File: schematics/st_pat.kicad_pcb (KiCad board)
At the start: 2 copper layers, 23 parts, among them J4 BATTERY, SW1 SW_PWR, SW2 BTN_RST, SW3 BTN, SW4 BTN, SW5 BTN, U1 FGPMMOPA6H, U2 FEATHER_M0_BASIC_PROTO, U3 LIS2MDL_ADAFRUIT, U4 Sharp_Display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

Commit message: Re add routes
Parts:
- moved SW2 85.7 mm to (97.2, 93.3)
- moved U1 85.2 mm to (192.4, 77.5)
- moved C2 74.1 mm to (184.8, 62.9), turned to 270 degrees
- moved C1 71.5 mm to (181.0, 62.9), turned to 270 degrees
- moved D2 17.8 mm to (179.1, 93.8)
- moved R2 17.8 mm to (186.7, 94.2)
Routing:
- net +3V3: track 0.00 -> 271.3 mm
- net /RST: track 0.00 -> 202.6 mm
- net /MOSI: track 0.00 -> 174.1 mm, vias 0 -> 2
- net /SCK: track 0.00 -> 170.4 mm, vias 0 -> 2
- net /MISO: track 0.00 -> 153.8 mm, vias 0 -> 2
- net /GPS_FIX_D11: track 0.00 -> 116.5 mm
- net /GPS_TX: track 0.00 -> 100.1 mm, vias 0 -> 1
- net /GPS_RX: track 0.00 -> 99.3 mm, vias 0 -> 1
- net /CPS_CS_D10: track 0.00 -> 78.8 mm
- net /SRAD_RECV_CS_A5: track 0.00 -> 70.9 mm
- net +BATT: track 0.00 -> 56.7 mm
- net /COTS_RECV_CS_A4: track 0.00 -> 54.9 mm
- net /BTN_A3: track 0.00 -> 51.7 mm
- net /GPS_PPS_D12: track 0.00 -> 41.8 mm
- net /BTN_A2: track 0.00 -> 34.4 mm
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
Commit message: fix board outline
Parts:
- moved   0.46 mm to (189.5, 40.6)
- moved   0.38 mm to (89.9, 121.4)
- moved   0.38 mm to (89.9, 40.6)
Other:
- board outline added: 106.7 x 87 mm
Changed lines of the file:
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@@
       (outputformat 1)
       (mirror false)
-      (drillshape 1)
+      (drillshape 0)
       (scaleselection 1)
-      (outputdirectory ""))
+      (outputdirectory "./"))
   )
   (net 0 "")
@@
   )
   (module MountingHole:MountingHole_2.5mm_Pad (layer F.Cu)
-    (at 89.535 121.412)
+    (at 89.916 121.412)
     (descr "Mounting Hole 2.5mm")
     (tags "mounting hole 2.5mm")
@@
   )
   (module MountingHole:MountingHole_2.5mm_Pad (layer F.Cu)
-    (at 89.535 40.64)
+    (at 89.916 40.64)
     (descr "Mounting Hole 2.5mm")
     (tags "mounting hole 2.5mm")
@@
   )
   (module MountingHole:MountingHole_2.5mm_Pad (layer F.Cu)
-    (at 189.865 40.386)
+    (at 189.484 40.64)
     (descr "Mounting Hole 2.5mm")
     (tags "mounting hole 2.5mm")
@@
       (effects (font (size 0.5 0.5) (thickness 0.08)))
     )
-    (pad 1 smd roundrect (at -1 0) (size 1.2 1.4) (layers F.Cu F.Paste F.Mask) (roundrect_rratio 0.208333)
+    (pad 1 smd roundrect (at -1 0) (size 1.2 1.4) (layers F.Cu F.Paste F.Mask) (roundrect_rratio 0.2083325)
       (net 19 "Net-(D3-Pad1)"))
-    (pad 2 smd roundrect (at 1 0) (size 1.2 1.4) (layers F.Cu F.Paste F.Mask) (roundrect_rratio 0.208333)
+    (pad 2 smd roundrect (at 1 0) (size 1.2 1.4) (layers F.Cu F.Paste F.Mask) (roundrect_rratio 0.2083325)
       (net 1 GND))
     (model ${KISYS3DMOD}/Resistor_SMD.3dshapes/R_0805_2012Metric.wrl
@@
       (effects (font (size 0.8 0.8) (thickness 0.12)))
     )
-    (pad 1 smd roundrect (at -1.4875 0 90) (size 1.425 1.75) (layers F.Cu F.Paste F.Mask) (roundrect_rratio 0.175439)
+    (pad 1 smd roundrect (at -1.4875 0 90) (size 1.425 1.75) (layers F.Cu F.Paste F.Mask) (roundrect_rratio 0.1754385964912281)
       (net 19 "Net-(D3-Pad1)"))
-    (pad 2 smd roundrect (at 1.4875 0 90) (size 1.425 1.75) (layers F.Cu F.Paste F.Mask) (roundrect_rratio 0.175439)
+    (pad 2 smd roundrect (at 1.4875 0 90) (size 1.425 1.75) (layers F.Cu F.Paste F.Mask) (roundrect_rratio 0.1754385964912281)
       (net 18 "Net-(D3-Pad2)"))
     (model ${KISYS3DMOD}/LED_SMD.3dshapes/LED_1206_3216Metric.wrl
@@
       (effects (font (size 0.5 0.5) (thickness 0.08)))
     )
-    (pad 2 smd roundrect (at 1 0 90) (size 1.2 1.4) (layers F.Cu F.Paste F.Mask) (roundrect_rratio 0.208333)
-      (net 1 GND))
-    (pad 1 smd roundrect (at -1 0 90) (size 1.2 1.4) (layers F.Cu F.Paste F.Mask) (roundrect_rratio 0.208333)
+    (pad 2 smd roundrect (at 1 0 90) (size 1.2 1.4) (layers F.Cu F.Paste F.Mask) (roundrect_rratio 0.2083325)
+      (net 1 GND))
+    (pad 1 smd roundrect (at -1 0 90) (size 1.2 1.4) (layers F.Cu F.Paste F.Mask) (roundrect_rratio 0.2083325)
       (net 5 "Net-(D2-Pad1)"))
     (model ${KISYS3DMOD}/Resistor_SMD.3dshapes/R_0805_2012Metric.wrl
@@
       (effects (font (size 0.5 0.5) (thickness 0.08)))
     )
-    (pad 1 smd roundrect (at -1 0) (size 1.2 1.4) (layers F.Cu F.Paste F.Mask) (roundrect_rratio 0.208333)
+    (pad 1 smd roundrect (at -1 0) (size 1.2 1.4) (layers F.Cu F.Paste F.Mask) (roundrect_rratio 0.2083325)
       (net 4 "Net-(D1-Pad1)"))
-    (pad 2 smd roundrect (at 1 0) (size 1.2 1.4) (layers F.Cu F.Paste F.Mask) (roundrect_rratio 0.208333)
+    (pad 2 smd roundrect (at 1 0) (size 1.2 1.4) (layers F.Cu F.Paste F.Mask) (roundrect_rratio 0.2083325)
       (net 1 GND))
     (model ${KISYS3DMOD}/Resistor_SMD.3dshapes/R_0805_2012Metric.wrl
@@
       (effects (font (size 0.8 0.8) (thickness 0.12)))
     )
-    (pad 2 smd roundrect (at 1.4875 0 90) (size 1.425 1.75) (layers F.Cu F.Paste F.Mask) (roundrect_rratio 0.175439)
+    (pad 2 smd roundrect (at 1.4875 0 90) (size 1.425 1.75) (layers F.Cu F.Paste F.Mask) (roundrect_rratio 0.1754385964912281)
       (net 2 +3V3))
-    (pad 1 smd roundrect (at -1.4875 0 90) (size 1.425 1.75) (layers F.Cu F.Paste F.Mask) (roundrect_rratio 0.175439)
+    (pad 1 smd roundrect (at -1.4875 0 90) (size 1.425 1.75) (layers F.Cu F.Paste F.Mask) (roundrect_rratio 0.1754385964912281)
       (net 5 "Net-(D2-Pad1)"))
     (model ${KISYS3DMOD}/LED_SMD.3dshapes/LED_1206_3216Metric.wrl
@@
       (effects (font (size 0.8 0.8) (thickness 0.12)))
     )
-    (pad 1 smd roundrect (at -1.4875 0 90) (size 1.425 1.75) (layers F.Cu F.Paste F.Mask) (roundrect_rratio 0.175439)
+    (pad 1 smd roundrect (at -1.4875 0 90) (size 1.425 1.75) (layers F.Cu F.Paste F.Mask) (roundrect_rratio 0.1754385964912281)
       (net 4 "Net-(D1-Pad1)"))
-    (pad 2 smd roundrect (at 1.4875 0 90) (size 1.425 1.75) (layers F.Cu F.Paste F.Mask) (roundrect_rratio 0.175439)
+    (pad 2 smd roundrect (at 1.4875 0 90) (size 1.425 1.75) (layers F.Cu F.Paste F.Mask) (roundrect_rratio 0.1754385964912281)
       (net 3 /GPS_FIX_D11))
     (model ${KISYS3DMOD}/LED_SMD.3dshapes/LED_1206_3216Metric.wrl
@@
       (effects (font (size 0.5 0.5) (thickness 0.08)))
     )
-    (pad 1 smd roundrect (at -1.0375 0 270) (size 1.175 1.45) (layers F.Cu F.Paste F.Mask) (roundrect_rratio 0.212766)
+    (pad 1 smd roundrect (at -1.0375 0 270) (size 1.175 1.45) (layers F.Cu F.Paste F.Mask) (roundrect_rratio 0.2127659574468085)
       (net 2 +3V3))
-    (pad 2 smd roundrect (at 1.0375 0 270) (size 1.175 1.45) (layers F.Cu F.Paste F.Mask) (roundrect_rratio 0.212766)
+    (pad 2 smd roundrect (at 1.0375 0 270) (size 1.175 1.45) (layers F.Cu F.Paste F.Mask) (roundrect_rratio 0.2127659574468085)
       (net 1 GND))
     (model ${KISYS3DMOD}/Capacitor_SMD.3dshapes/C_0805_2012Metric.wrl
@@
       (effects (font (size 0.5 0.5) (thickness 0.08)))
     )
-    (pad 1 smd roundrect (at -1.0375 0 270) (size 1.175 1.45) (layers F.Cu F.Paste F.Mask) (roundrect_rratio 0.212766)
+    (pad 1 smd roundrect (at -1.0375 0 270) (size 1.175 1.45) (layers F.Cu F.Paste F.Mask) (roundrect_rratio 0.2127659574468085)
       (net 2 +3V3))
-    (pad 2 smd roundrect (at 1.0375 0 270) (size 1.175 1.45) (layers F.Cu F.Paste F.Mask) (roundrect_rratio 0.212766)
+    (pad 2 smd roundrect (at 1.0375 0 270) (size 1.175 1.45) (layers F.Cu F.Paste F.Mask) (roundrect_rratio 0.2127659574468085)
       (net 1 GND))
     (model ${KISYS3DMOD}/Capacitor_SMD.3dshapes/C_0805_2012Metric.wrl
@@
     (pad 2 thru_hole oval (at 2 0 180) (size 1.2 1.75) (drill 0.75) (layers *.Cu *.Mask)
       (net 1 GND))
-    (pad 1 thru_hole roundrect (at 0 0 180) (size 1.2 1.75) (drill 0.75) (layers *.Cu *.Mask) (roundrect_rratio 0.208333)
+    (pad 1 thru_hole roundrect (at 0 0 180) (size 1.2 1.75) (drill 0.75) (layers *.Cu *.Mask) (roundrect_rratio 0.2083325)
       (net 17 "Net-(J4-Pad1)"))
     (model ${KISYS3DMOD}/Connector_JST.3dshapes/JST_PH_S2B-PH-K_1x02_P2.00mm_Horizontal.wrl
@@
     )
   )
-  (gr_line (start 193.04 37.465) (end 193.04 124.46) (layer Dwgs.User) (width 0.15))
-  (gr_line (start 86.36 124.46) (end 86.36 37.465) (layer Dwgs.User) (width 0.15))
-  (gr_line (start 193.04 124.46) (end 86.36 124.46) (layer Dwgs.User) (width 0.15))
-  (gr_line (start 86.36 37.465) (end 193.04 37.465) (layer Dwgs.User) (width 0.15))
+  (gr_line (start 86.36 124.46) (end 86.36 37.465) (layer Edge.Cuts) (width 0.15))
+  (gr_line (start 193.04 124.46) (end 86.36 124.46) (layer Edge.Cuts) (width 0.15))
+  (gr_line (start 86.36 37.465) (end 193.04 37.465) (layer Edge.Cuts) (width 0.15))
+  (gr_line (start 193.04 37.465) (end 193.04 124.46) (layer Edge.Cuts) (width 0.15))
   (via (at 141.478 83.566) (size 0.8) (drill 0.4) (layers F.Cu B.Cu) (net 1))
   (via (at 174.498 82.55) (size 0.8) (drill 0.4) (layers F.Cu B.Cu) (net 1))

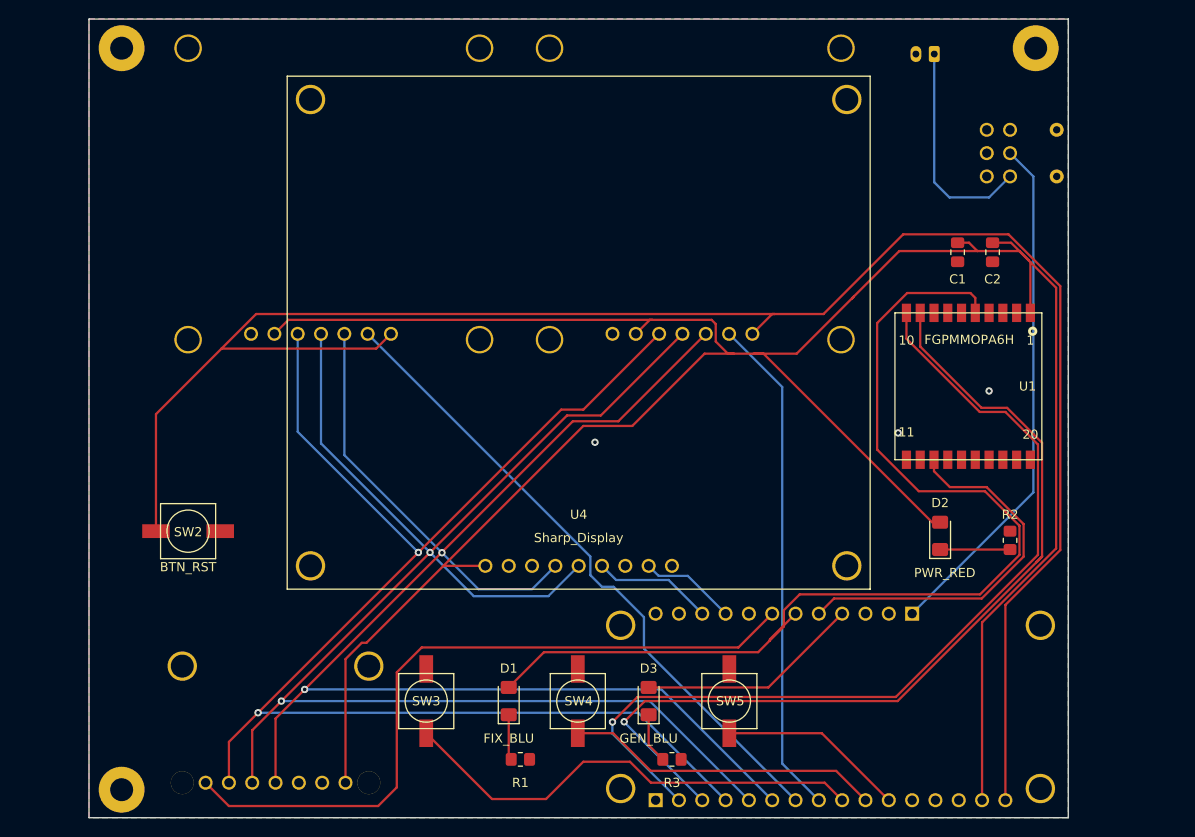
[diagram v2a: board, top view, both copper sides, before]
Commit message: redo board layout
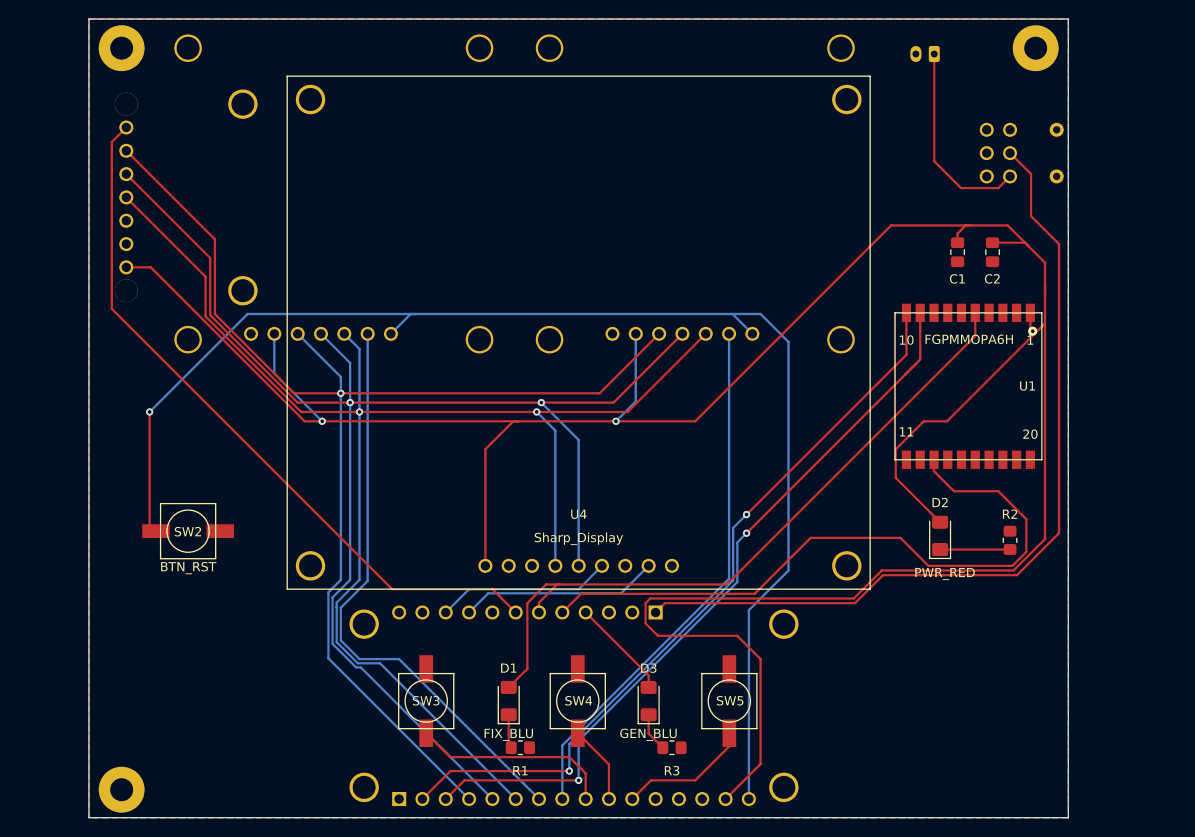
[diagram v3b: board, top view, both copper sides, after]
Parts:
- moved U3 41.0 mm to (108.2, 62.0), turned to 90 degrees
- moved U2 27.9 mm to (139.2, 112.3)
- moved R1 1.27 mm to (133.3, 116.8)
- moved R3 1.27 mm to (149.9, 116.8)
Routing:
- net /RST: track 202.6 -> 146.7 mm, vias 0 -> 1
- net /GPS_FIX_D11: track 116.5 -> 77.6 mm
- net +3V3: track 271.3 -> 309.4 mm, vias 0 -> 2
- net +BATT: track 56.7 -> 91.1 mm
- net /GPS_PPS_D12: track 41.8 -> 72.8 mm
- net /BTN_A3: track 51.7 -> 22.0 mm
- net /BTN_A2: track 34.4 -> 8.58 mm
- net /MISO: track 153.8 -> 135.9 mm, vias 2 -> 1
- net /GPS_RX: track 99.3 -> 82.4 mm, vias 1 -> 2
- net /GPS_TX: track 100.1 -> 83.3 mm, vias 1 -> 2
- net /MOSI: track 174.1 -> 157.4 mm
- net Net-(D3-Pad2): track 24.4 -> 11.0 mm
- net /SCK: track 170.4 -> 158.5 mm
- net /SHARP_DISP_D6: track 10.5 -> 21.7 mm
- net /SRAD_RECV_CS_A5: track 70.9 -> 63.4 mm
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
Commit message: fix pr issues
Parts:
- U3: moved to F.Cu
- U4: value Sharp_Display -> Sharp_Display_4694
- U5: value Telemetry_Breakout -> COTS_GPS_RECEIVER
- U6: value Telemetry_Breakout -> SRAD_GPS_RECEIVER
- moved U3 9.91 mm to (108.2, 52.1), turned to 270 degrees
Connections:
- SW1 pad 1: (no net) -> Net-(SW1-Pad1)
- SW1 pad 2: (no net) -> Net-(SW1-Pad2)
- SW1 pad 3: (no net) -> Net-(SW1-Pad3)
- SW1 pad 4: (no net) -> Net-(SW1-Pad4)
- U1 pad 11: (no net) -> Net-(U1-Pad11)
- U1 pad 14: (no net) -> Net-(U1-Pad14)
- U1 pad 15: (no net) -> Net-(U1-Pad15)
- U1 pad 16: (no net) -> Net-(U1-Pad16)
- U1 pad 17: (no net) -> Net-(U1-Pad17)
- U1 pad 18: (no net) -> Net-(U1-Pad18)
- U1 pad 2: (no net) -> Net-(U1-Pad2)
- U1 pad 20: (no net) -> Net-(U1-Pad20)
- U1 pad 4: (no net) -> Net-(U1-Pad4)
- U1 pad 6: (no net) -> Net-(U1-Pad6)
- U1 pad 7: (no net) -> Net-(U1-Pad7)
- U2 pad P1_12: (no net) -> Net-(U2-PadP1_12)
- U2 pad P1_14: (no net) -> Net-(U2-PadP1_14)
- U2 pad P2_11: (no net) -> Net-(U2-PadP2_11)
- U2 pad P2_12: (no net) -> Net-(U2-PadP2_12)
- U2 pad P2_2: (no net) -> Net-(U2-PadP2_2)
- U2 pad P2_3: (no net) -> Net-(U2-PadP2_3)
- U2 pad P2_8: (no net) -> Net-(U2-PadP2_8)
- U3 pad 2: (no net) -> Net-(U3-Pad2)
- U4 pad 2: (no net) -> Net-(U4-Pad2)
- U4 pad 7: (no net) -> Net-(U4-Pad7)
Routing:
- net /CPS_CS_D10: track 78.1 -> 64.3 mm
- net +3V3: track 309.4 -> 319.6 mm, vias 2 -> 1
- net /RST: track 146.7 -> 138.4 mm
- net /SRAD_RECV_CS_A5: track 63.4 -> 70.6 mm
- net /SCK: track 158.5 -> 164.1 mm
- net /MISO: track 135.9 -> 130.7 mm
- net /MOSI: track 157.4 -> 159.7 mm

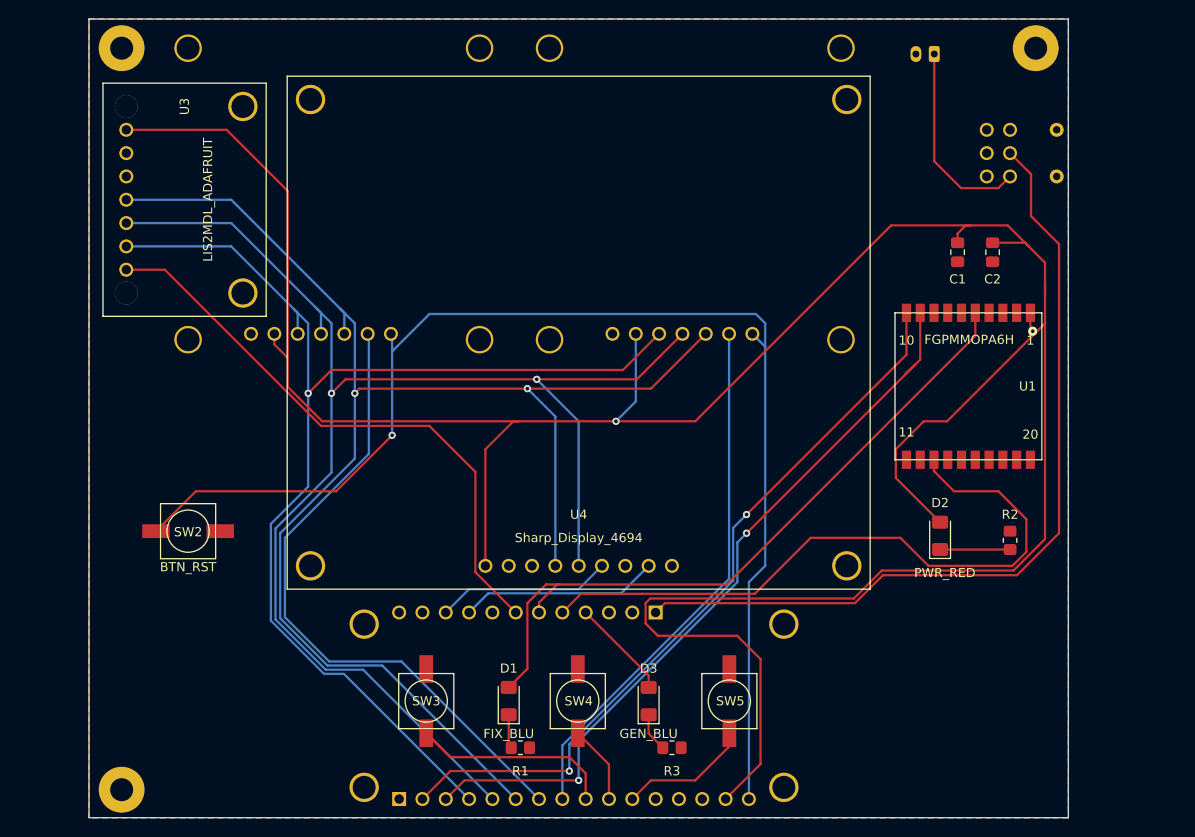
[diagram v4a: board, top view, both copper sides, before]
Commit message: wip replacing gps module with breakout
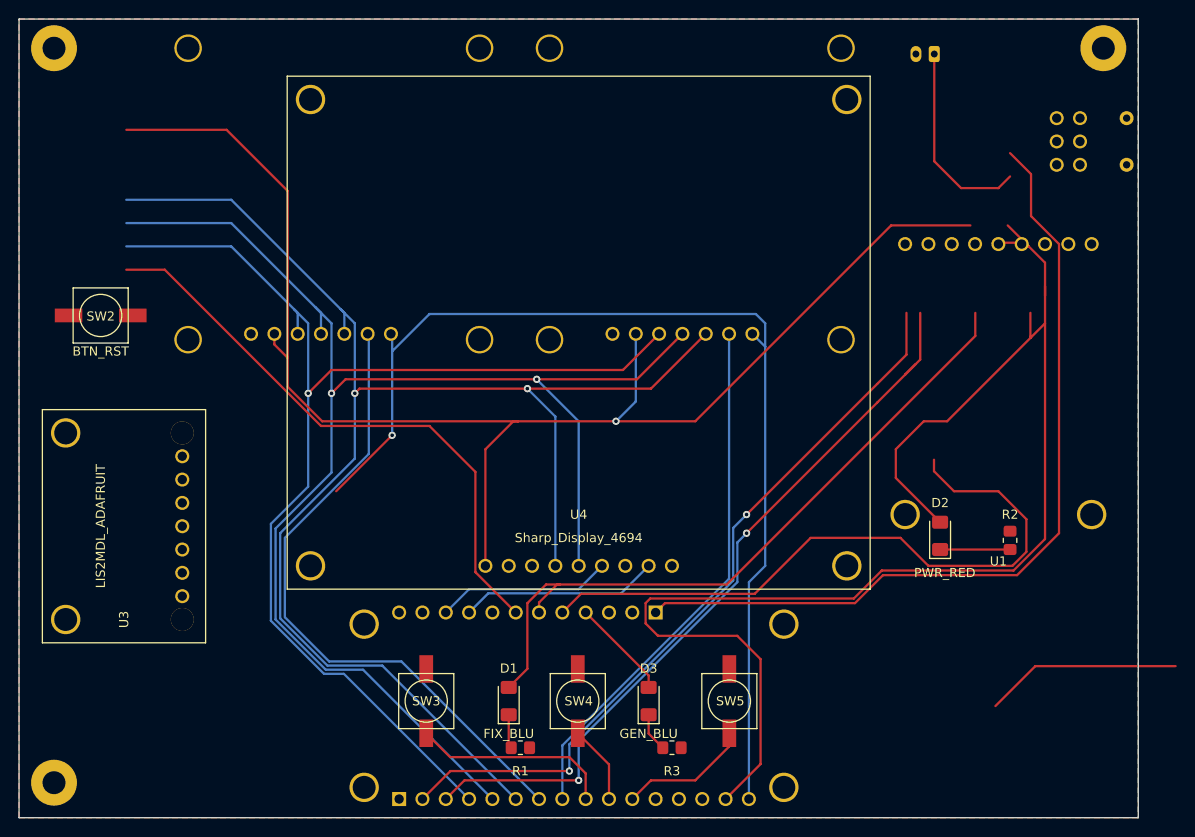
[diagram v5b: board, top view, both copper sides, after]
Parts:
- removed C1: 1uF, Capacitor_SMD:C_0805_2012Metric_Pad1.18x1.45mm_HandSolder
- removed C2: 0.01uF, Capacitor_SMD:C_0805_2012Metric_Pad1.18x1.45mm_HandSolder
- U1: value FGPMMOPA6H -> GPS_Breakout_746; footprint st_pat:FGPMMOPA6H -> st_pat:GPS_Breakout_746
- moved U3 54.4 mm to (78.7, 97.8), turned to 90 degrees
- moved SW2 25.4 mm to (87.6, 69.8)
- moved U1 20.8 mm to (185.4, 97.0), turned to 180 degrees
- moved SW1 7.73 mm to (191.8, 48.3)
- moved   7.41 mm to (82.5, 120.7)
- moved   7.37 mm to (82.5, 40.6)
- moved   7.37 mm to (196.8, 40.6)
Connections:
- U1 pad 1: +3V3 -> /GPS_PPS_D12
- U1 pad 4: Net-(U1-Pad4) -> /GPS_RX
- U1 pad 5: /GPS_FIX_D11 -> /GPS_TX
- U1 pad 6: Net-(U1-Pad6) -> /GPS_FIX_D11
- U1 pad 8: GND -> Net-(U1-Pad8)
- U1 pad 9: /GPS_TX -> +3V3
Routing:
- net +3V3: track 319.6 -> 312.8 mm
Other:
- board size 106.7 x 87 mm -> 121.9 x 87 mm

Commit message: wip: redo layout and use diffrent button footprint
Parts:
- removed D1: FIX_BLU, LED_SMD:LED_1206_3216Metric_Pad1.42x1.75mm_HandSolder
- removed R1: 100, Resistor_SMD:R_0805_2012Metric_Pad1.20x1.40mm_HandSolder
- SW2, SW3, SW4, SW5: footprint st_pat:SW_Mini_Soft -> Button_Switch_THT:SW_PUSH_6mm
- moved R2 61.2 mm to (129.8, 116.8), turned to 180 degrees
- moved D2 50.3 mm to (132.1, 111.7)
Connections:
- SW1 pad 1: Net-(SW1-Pad1) -> (no net)
- SW1 pad 2: Net-(SW1-Pad2) -> (no net)
- SW1 pad 3: Net-(SW1-Pad3) -> (no net)
- SW1 pad 4: Net-(SW1-Pad4) -> (no net)
- U1 pad 2: Net-(U1-Pad2) -> (no net)
- U1 pad 7: Net-(U1-Pad7) -> (no net)
- U1 pad 8: Net-(U1-Pad8) -> (no net)
- U2 pad P1_12: Net-(U2-PadP1_12) -> (no net)
- U2 pad P1_14: Net-(U2-PadP1_14) -> (no net)
- U2 pad P2_11: Net-(U2-PadP2_11) -> (no net)
- U2 pad P2_12: Net-(U2-PadP2_12) -> (no net)
- U2 pad P2_2: Net-(U2-PadP2_2) -> (no net)
- U2 pad P2_3: Net-(U2-PadP2_3) -> (no net)
- U2 pad P2_8: Net-(U2-PadP2_8) -> (no net)
- U3 pad 2: Net-(U3-Pad2) -> (no net)
- U4 pad 2: Net-(U4-Pad2) -> (no net)
- U4 pad 7: Net-(U4-Pad7) -> (no net)
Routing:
- net +3V3: track 312.8 -> 341.4 mm, vias 1 -> 0
- net /GPS_RX: track 82.4 -> 93.0 mm
- net /MOSI: track 159.7 -> 149.5 mm
- net /SCK: track 164.1 -> 154.2 mm
- net /MISO: track 130.7 -> 120.9 mm
- net /GPS_TX: track 83.3 -> 92.7 mm
- net /GPS_PPS_D12: track 72.8 -> 64.7 mm
- net Net-(J4-Pad1): track 21.7 -> 27.8 mm
- net Net-(D1-Pad1): track 4.09 -> 0.00 mm
- net Net-(D2-Pad1): track 7.62 -> 4.16 mm
- net /CPS_CS_D10: track 64.3 -> 60.9 mm
- net /GPS_FIX_D11: track 77.6 -> 80.8 mm
- net /RST: track 138.4 -> 135.4 mm, vias 1 -> 0
